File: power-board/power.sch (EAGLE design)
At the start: 2 parts, among them IC1 7805TV

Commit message: pow
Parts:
- added C1, C2, C3, C4: 100 nF, resistor:C-EU025-025X050
- added D1: (no value), SparkFun-LED:LED5MM
- added R1: 470, resistor:R-EU_0207/10
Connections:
- new net N$1: IC1.VI, JP1.GND, R1.1
- new net N$2: D1.C, IC1.GND, JP1.PWR
- new net N$3: D1.A, R1.2
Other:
- moved on the sheet: IC1
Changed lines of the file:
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@@
 <part name="JP1" library="SparkFun-Connectors" deviceset="POWER_JACK" device="PTH_LOCK"/>
 <part name="IC1" library="linear" deviceset="78*" device="TV" technology="05"/>
+<part name="D1" library="SparkFun-LED" deviceset="LED" device="5MM"/>
+<part name="R1" library="resistor" deviceset="R-EU_" device="0207/10" value="470"/>
+<part name="C1" library="resistor" deviceset="C-EU" device="025-025X050" value="100 nF"/>
+<part name="C2" library="resistor" deviceset="C-EU" device="025-025X050" value="100 nF"/>
+<part name="C3" library="resistor" deviceset="C-EU" device="025-025X050" value="100 nF"/>
+<part name="C4" library="resistor" deviceset="C-EU" device="025-025X050" value="100 nF"/>
 </parts>
 <sheets>
@@
 <attribute name="NAME" x="38.1" y="60.96" size="1.778" layer="95"/>
 </instance>
-<instance part="IC1" gate="A1" x="78.74" y="68.58"/>
+<instance part="IC1" gate="A1" x="63.5" y="45.72"/>
+<instance part="D1" gate="G$1" x="73.66" y="66.04" rot="R180"/>
+<instance part="R1" gate="G$1" x="68.58" y="63.5"/>
+<instance part="C1" gate="G$1" x="50.8" y="43.18"/>
+<instance part="C2" gate="G$1" x="76.2" y="43.18"/>
+<instance part="C3" gate="G$1" x="81.28" y="43.18"/>
+<instance part="C4" gate="G$1" x="86.36" y="43.18"/>
 </instances>
 <busses>
 </busses>
 <nets>
+<net name="N$1" class="0">
+<segment>
+<pinref part="JP1" gate="G$1" pin="GND"/>
+<pinref part="IC1" gate="A1" pin="VI"/>
+<wire x1="50.8" y1="63.5" x2="63.5" y2="63.5" width="0.1524" layer="91"/>
+<wire x1="63.5" y1="63.5" x2="53.34" y2="45.72" width="0.1524" layer="91"/>
+<pinref part="R1" gate="G$1" pin="1"/>
+<junction x="63.5" y="63.5"/>
+</segment>
+</net>
+<net name="N$2" class="0">
+<segment>
+<pinref part="JP1" gate="G$1" pin="PWR"/>
+<wire x1="50.8" y1="68.58" x2="58.42" y2="68.58" width="0.1524" layer="91"/>
+<wire x1="58.42" y1="68.58" x2="58.42" y2="60.96" width="0.1524" layer="91"/>
+<pinref part="IC1" gate="A1" pin="GND"/>
+<wire x1="58.42" y1="60.96" x2="63.5" y2="38.1" width="0.1524" layer="91"/>
+<pinref part="D1" gate="G$1" pin="C"/>
+<wire x1="73.66" y1="71.12" x2="58.42" y2="71.12" width="0.1524" layer="91"/>
+<wire x1="58.42" y1="71.12" x2="58.42" y2="68.58" width="0.1524" layer="91"/>
+</segment>
+</net>
+<net name="N$3" class="0">
+<segment>
+<pinref part="R1" gate="G$1" pin="2"/>
+<pinref part="D1" gate="G$1" pin="A"/>
+</segment>
+</net>
 </nets>
 </sheet>

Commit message: power board ok
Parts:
- removed C3, C4: 100 nF, resistor:C-EU025-025X050
- added ARDU: (no value), pinhead:PINHD-1X3
- added DISPLAY, LED: (no value), pinhead:PINHD-1X2
- added FOTOC: (no value), pinhead:PINHD-1X4
- C2: value 100 nF -> 330 nF
- JP1: value POWER_JACKPTH_LOCK -> POWER_JACKPTH; device SparkFun-Connectors:POWER_JACKPTH_LOCK -> SparkFun-Connectors:POWER_JACKPTH
- R1: value 470 -> 680
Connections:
- removed net N$3: D1.A, R1.2
- new net N$5: ARDU.3, C1.2, C2.1, DISPLAY.2, FOTOC.3, FOTOC.4, IC1.GND, JP1.GND, LED.2, R1.1
- new net N$6: C1.1, DISPLAY.1, IC1.VO, LED.1
- net N$1: now also D1.C, R1.2; no longer IC1.VI, JP1.GND, R1.1
- net N$2: now also ARDU.1, C2.2, D1.A, FOTOC.1, FOTOC.2, IC1.VI; no longer D1.C, IC1.GND
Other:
- moved on the sheet: C1, C2, D1, IC1, JP1, R1

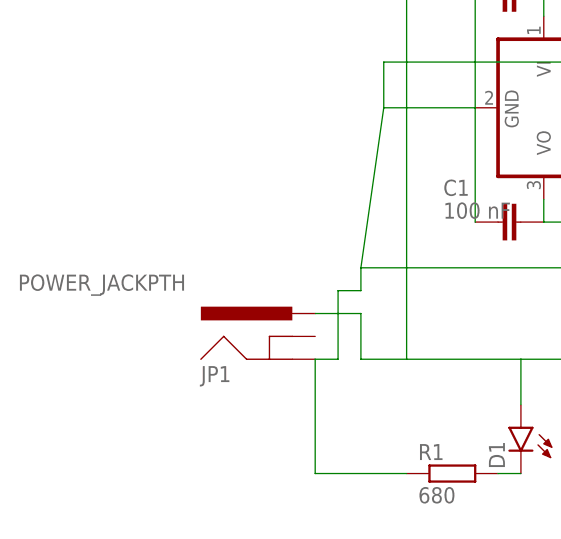
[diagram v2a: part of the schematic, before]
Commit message: Power board printed
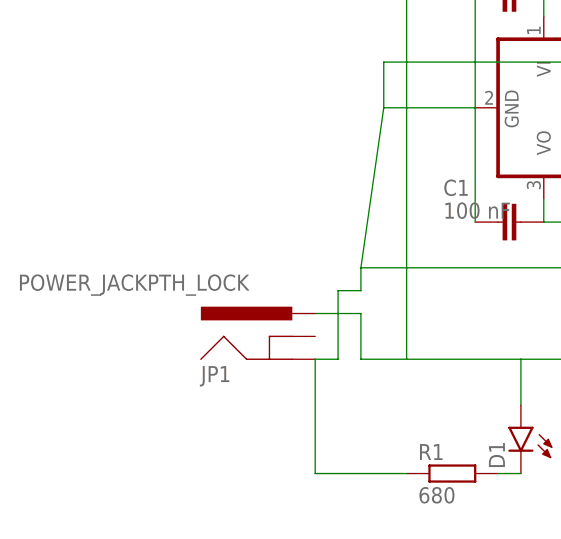
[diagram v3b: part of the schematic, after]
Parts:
- JP1: value POWER_JACKPTH -> POWER_JACKPTH_LOCK; device SparkFun-Connectors:POWER_JACKPTH -> SparkFun-Connectors:POWER_JACKPTH_LOCK
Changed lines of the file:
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@@
 </classes>
 <parts>
-<part name="JP1" library="SparkFun-Connectors" deviceset="POWER_JACK" device="PTH" value="POWER_JACKPTH"/>
+<part name="JP1" library="SparkFun-Connectors" deviceset="POWER_JACK" device="PTH_LOCK" value="POWER_JACKPTH_LOCK"/>
 <part name="IC1" library="linear" deviceset="78*" device="TV" technology="05"/>
 <part name="D1" library="SparkFun-LED" deviceset="LED" device="5MM"/>

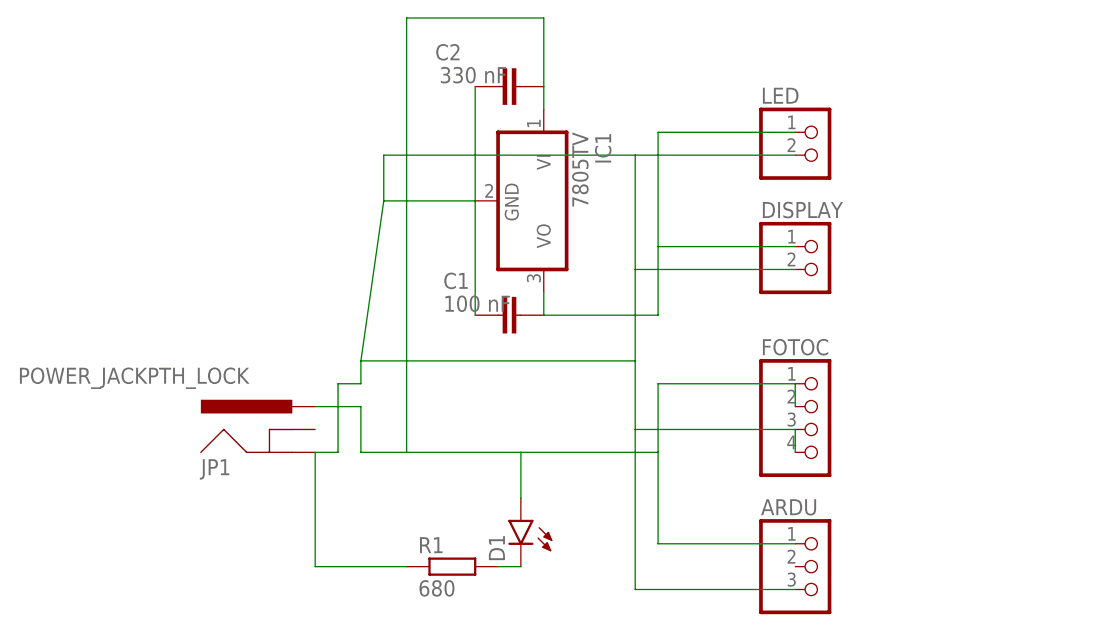
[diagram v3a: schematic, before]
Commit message: Learned how to use net (instead of wires) cleaned connections in schematic made ground plane a real GND routed like a boss \m/
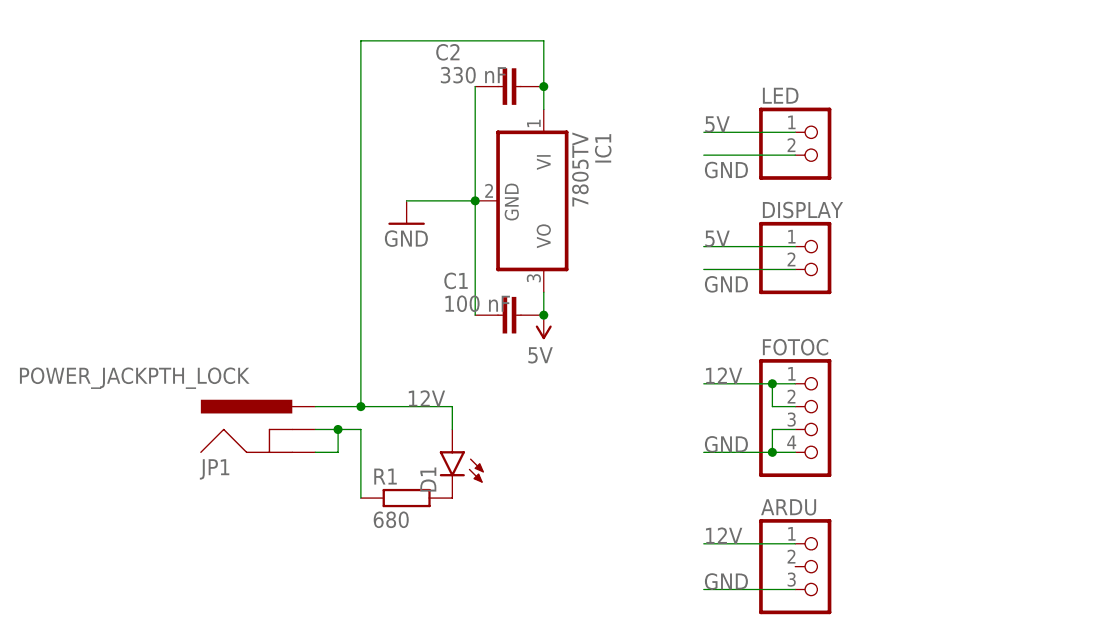
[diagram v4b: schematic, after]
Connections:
- net N$2 renamed 12V
- net N$6 renamed 5V
- removed net N$5: ARDU.3, C1.2, C2.1, DISPLAY.2, FOTOC.3, FOTOC.4, IC1.GND, JP1.GND, LED.2, R1.1
- new net GND: ARDU.3, C1.2, C2.1, DISPLAY.2, FOTOC.3, FOTOC.4, IC1.GND, JP1.GND, JP1.GNDBREAK, LED.2, R1.1
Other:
- moved on the sheet: D1, R1
